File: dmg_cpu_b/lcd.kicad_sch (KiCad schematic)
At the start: 120 parts

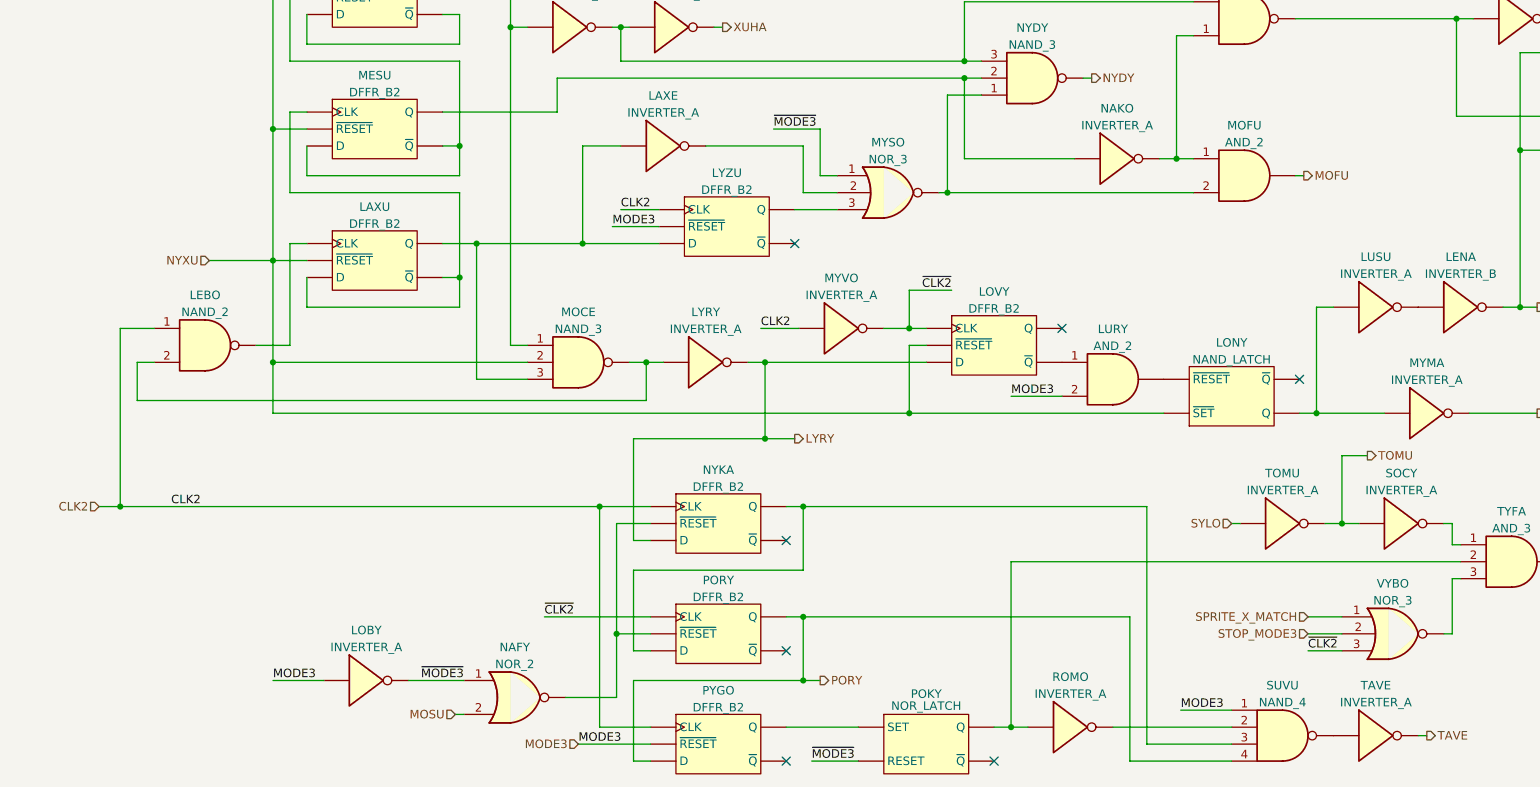
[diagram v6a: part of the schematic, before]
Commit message: More OAM sheets added.
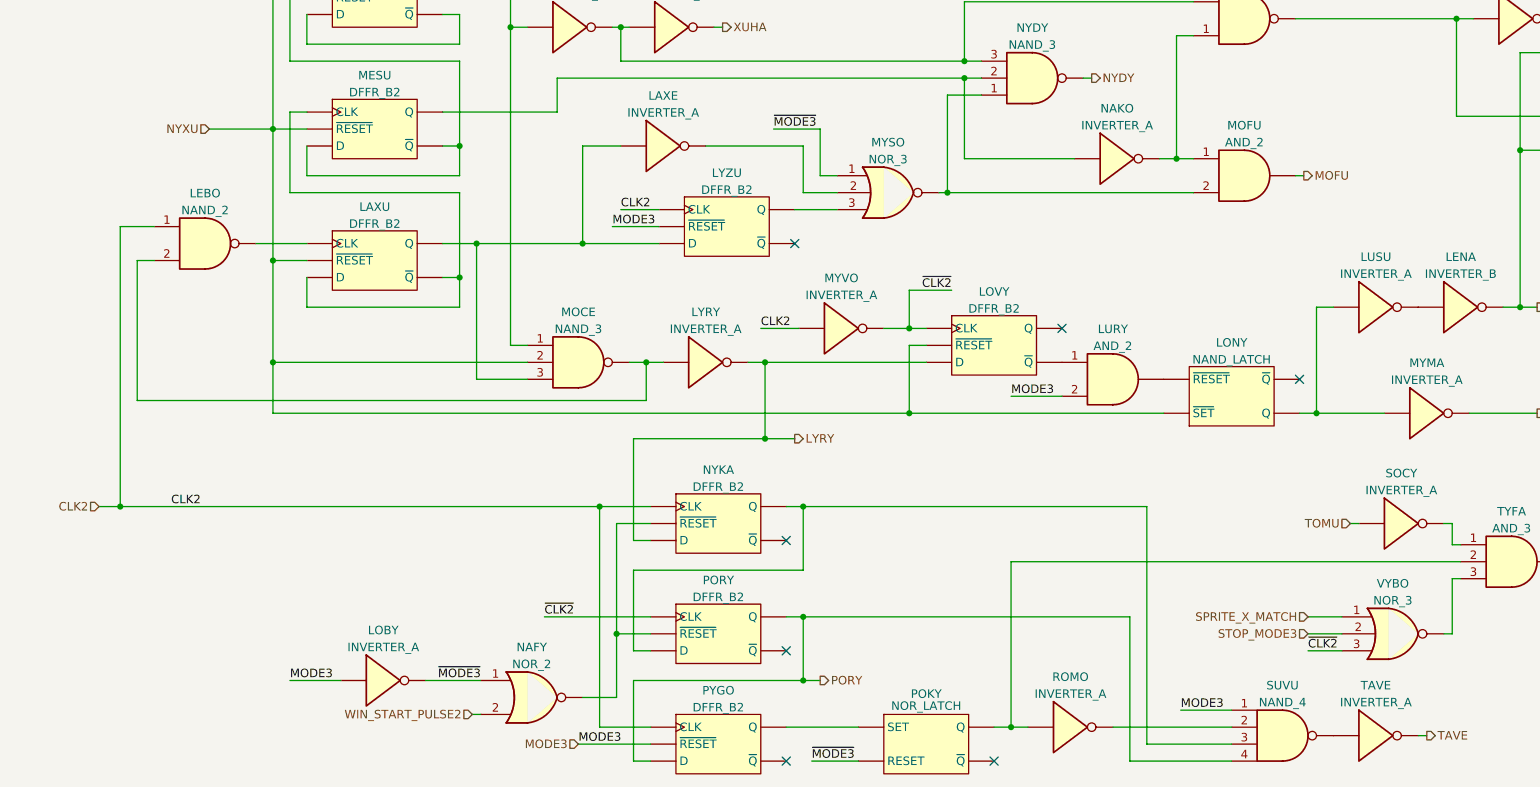
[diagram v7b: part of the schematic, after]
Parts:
- removed TOMU: INVERTER_A, symbol DMG_CPU_Cells:INVERTER_A
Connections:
- net MOSU renamed WIN_START_PULSE2
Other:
- moved on the sheet: LEBO, LOBY, NAFY
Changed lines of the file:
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@@
   (junction (at 331.47 94.615) (diameter 0) (color 0 0 0 0)
   )
-  (junction (at 208.28 245.745) (diameter 0) (color 0 0 0 0)
-  )
   (junction (at 127.635 269.24) (diameter 0) (color 0 0 0 0)
   )
@@
     (stroke (width 0) (type default) (color 0 0 0 0))
   )
-  (wire (pts (xy 50.8 203.835) (xy 50.8 219.075))
-    (stroke (width 0) (type default) (color 0 0 0 0))
-  )
   (wire (pts (xy 124.46 121.285) (xy 129.54 121.285))
     (stroke (width 0) (type default) (color 0 0 0 0))
@@
     (stroke (width 0) (type default) (color 0 0 0 0))
   )
-  (wire (pts (xy 76.835 274.32) (xy 75.565 274.32))
+  (wire (pts (xy 79.375 274.32) (xy 78.105 274.32))
     (stroke (width 0) (type default) (color 0 0 0 0))
   )
@@
     (stroke (width 0) (type default) (color 0 0 0 0))
   )
-  (wire (pts (xy 27.94 221.615) (xy 27.94 227.33))
+  (wire (pts (xy 27.94 206.375) (xy 27.94 227.33))
     (stroke (width 0) (type default) (color 0 0 0 0))
   )
@@
     (stroke (width 0) (type default) (color 0 0 0 0))
   )
-  (wire (pts (xy 38.735 206.375) (xy 48.26 206.375))
+  (wire (pts (xy 38.735 186.69) (xy 48.26 186.69))
     (stroke (width 0) (type default) (color 0 0 0 0))
   )
@@
     (stroke (width 0) (type default) (color 0 0 0 0))
   )
-  (wire (pts (xy 30.48 221.615) (xy 27.94 221.615))
+  (wire (pts (xy 30.48 206.375) (xy 27.94 206.375))
     (stroke (width 0) (type default) (color 0 0 0 0))
   )
@@
     (stroke (width 0) (type default) (color 0 0 0 0))
   )
-  (wire (pts (xy 208.28 245.745) (xy 210.82 245.745))
-    (stroke (width 0) (type default) (color 0 0 0 0))
-  )
   (wire (pts (xy 351.79 212.09) (xy 351.79 231.14))
     (stroke (width 0) (type default) (color 0 0 0 0))
@@
     (stroke (width 0) (type default) (color 0 0 0 0))
   )
-  (wire (pts (xy 53.34 203.835) (xy 50.8 203.835))
-    (stroke (width 0) (type default) (color 0 0 0 0))
-  )
   (wire (pts (xy 83.82 171.45) (xy 83.82 219.075))
     (stroke (width 0) (type default) (color 0 0 0 0))
@@
     (stroke (width 0) (type default) (color 0 0 0 0))
   )
-  (wire (pts (xy 191.77 245.745) (xy 193.04 245.745))
-    (stroke (width 0) (type default) (color 0 0 0 0))
-  )
   (wire (pts (xy 85.09 130.175) (xy 85.09 144.145))
     (stroke (width 0) (type default) (color 0 0 0 0))
@@
     (stroke (width 0) (type default) (color 0 0 0 0))
   )
-  (wire (pts (xy 208.28 235.585) (xy 212.09 235.585))
+  (wire (pts (xy 209.55 245.745) (xy 210.82 245.745))
     (stroke (width 0) (type default) (color 0 0 0 0))
   )
@@
     (stroke (width 0) (type default) (color 0 0 0 0))
   )
-  (wire (pts (xy 48.26 186.69) (xy 48.26 206.375))
-    (stroke (width 0) (type default) (color 0 0 0 0))
-  )
-  (wire (pts (xy 25.4 216.535) (xy 30.48 216.535))
+  (wire (pts (xy 25.4 201.295) (xy 30.48 201.295))
     (stroke (width 0) (type default) (color 0 0 0 0))
   )
@@
     (stroke (width 0) (type default) (color 0 0 0 0))
   )
-  (wire (pts (xy 92.075 271.78) (xy 99.695 271.78))
+  (wire (pts (xy 94.615 271.78) (xy 99.695 271.78))
     (stroke (width 0) (type default) (color 0 0 0 0))
   )
@@
     (stroke (width 0) (type default) (color 0 0 0 0))
   )
-  (wire (pts (xy 68.58 269.24) (xy 76.835 269.24))
+  (wire (pts (xy 71.12 269.24) (xy 79.375 269.24))
     (stroke (width 0) (type default) (color 0 0 0 0))
   )
@@
     (stroke (width 0) (type default) (color 0 0 0 0))
   )
-  (wire (pts (xy 50.8 219.075) (xy 45.72 219.075))
+  (wire (pts (xy 45.72 203.835) (xy 53.34 203.835))
     (stroke (width 0) (type default) (color 0 0 0 0))
   )
@@
     (stroke (width 0) (type default) (color 0 0 0 0))
   )
-  (wire (pts (xy 208.28 235.585) (xy 208.28 245.745))
-    (stroke (width 0) (type default) (color 0 0 0 0))
-  )
   (wire (pts (xy 183.515 88.9) (xy 183.515 128.27))
     (stroke (width 0) (type default) (color 0 0 0 0))
@@
     (stroke (width 0) (type default) (color 0 0 0 0))
   )
+  (wire (pts (xy 48.26 186.69) (xy 48.26 206.375))
+    (stroke (width 0) (type default) (color 0 0 0 0))
+  )
   (wire (pts (xy 186.055 196.215) (xy 149.225 196.215))
     (stroke (width 0) (type default) (color 0 0 0 0))
@@
     (stroke (width 0) (type default) (color 0 0 0 0))
   )
-  (wire (pts (xy 25.4 216.535) (xy 25.4 243.205))
+  (wire (pts (xy 25.4 201.295) (xy 25.4 243.205))
     (stroke (width 0) (type default) (color 0 0 0 0))
   )
@@
     (stroke (width 0) (type default) (color 0 0 0 0))
   )
-  (wire (pts (xy 205.74 245.745) (xy 208.28 245.745))
-    (stroke (width 0) (type default) (color 0 0 0 0))
-  )
   (wire (pts (xy 281.305 128.905) (xy 278.765 128.905))
     (stroke (width 0) (type default) (color 0 0 0 0))
@@
     (stroke (width 0) (type default) (color 0 0 0 0))
   )
-  (wire (pts (xy 48.26 269.24) (xy 55.88 269.24))
+  (wire (pts (xy 50.8 269.24) (xy 58.42 269.24))
     (stroke (width 0) (type default) (color 0 0 0 0))
   )
@@
     (effects (font (size 1.27 1.27)) (justify left bottom))
   )
-  (label "~{MODE3}" (at 76.835 269.24 180)
+  (label "~{MODE3}" (at 79.375 269.24 180)
     (effects (font (size 1.27 1.27)) (justify right bottom))
   )
@@
     (effects (font (size 1.27 1.27)) (justify left bottom))
   )
-  (label "MODE3" (at 48.26 269.24 0)
+  (label "MODE3" (at 50.8 269.24 0)
     (effects (font (size 1.27 1.27)) (justify left bottom))
   )
@@
     (effects (font (size 1.27 1.27)) (justify left bottom))
   )
-  (hierarchical_label "MOSU" (shape input) (at 75.565 274.32 180)
+  (hierarchical_label "WIN_START_PULSE2" (shape input) (at 78.105 274.32 180)
     (effects (font (size 1.27 1.27)) (justify right))
   )
@@
     (effects (font (size 1.27 1.27)) (justify right))
   )
-  (hierarchical_label "SYLO" (shape input) (at 191.77 245.745 180)
-    (effects (font (size 1.27 1.27)) (justify right))
-  )
   (hierarchical_label "CLKPIPE" (shape output) (at 279.4 254 0)
     (effects (font (size 1.27 1.27)) (justify left))
@@
     (effects (font (size 1.27 1.27)) (justify right))
   )
-  (hierarchical_label "NYXU" (shape input) (at 38.735 206.375 180)
+  (hierarchical_label "NYXU" (shape input) (at 38.735 186.69 180)
     (effects (font (size 1.27 1.27)) (justify right))
   )
@@
     (effects (font (size 1.27 1.27)) (justify left))
   )
-  (hierarchical_label "TOMU" (shape output) (at 212.09 235.585 0)
-    (effects (font (size 1.27 1.27)) (justify left))
+  (hierarchical_label "TOMU" (shape input) (at 209.55 245.745 180)
+    (effects (font (size 1.27 1.27)) (justify right))
   )
   (hierarchical_label "~{V_RESET}" (shape output) (at 314.96 22.225 0)
@@
     (pin "2")
   )
-  (symbol (lib_id "DMG_CPU_Cells:INVERTER_A") (at 199.39 245.745 0) (unit 1)
-    (in_bom yes) (on_board yes) (fields_autoplaced)
-    (property "Reference" "TOMU" (id 0) (at 199.39 238.2352 0))
-    (property "Value" "INVERTER_A" (id 1) (at 199.39 240.7721 0))
-    (property "Footprint" "" (id 2) (at 196.85 245.745 0)
-      (effects (font (size 1.27 1.27)) hide)
-    )
-    (property "Datasheet" "http://iceboy.a-singer.de/doc/dmg_cells.html#inv_a" (id 3) (at 200.66 253.365 0)
-      (effects (font (size 1.27 1.27)) hide)
-    )
-    (pin "1")
-    (pin "2")
-  )
   (symbol (lib_id "DMG_CPU_Cells:INVERTER_A") (at 314.325 119.38 0) (unit 1)
     (in_bom yes) (on_board yes)
@@
     (pin "6")
   )
-  (symbol (lib_id "DMG_CPU_Cells:INVERTER_A") (at 62.23 269.24 0) (unit 1)
+  (symbol (lib_id "DMG_CPU_Cells:INVERTER_A") (at 64.77 269.24 0) (unit 1)
     (in_bom yes) (on_board yes)
-    (property "Reference" "LOBY" (id 0) (at 62.23 261.7302 0))
-    (property "Value" "INVERTER_A" (id 1) (at 62.23 264.2671 0))
-    (property "Footprint" "" (id 2) (at 59.69 269.24 0)
+    (property "Reference" "LOBY" (id 0) (at 64.77 261.7302 0))
+    (property "Value" "INVERTER_A" (id 1) (at 64.77 264.2671 0))
+    (property "Footprint" "" (id 2) (at 62.23 269.24 0)
       (effects (font (size 1.27 1.27)) hide)
     )
-    (property "Datasheet" "http://iceboy.a-singer.de/doc/dmg_cells.html#inv_a" (id 3) (at 63.5 276.86 0)
+    (property "Datasheet" "http://iceboy.a-singer.de/doc/dmg_cells.html#inv_a" (id 3) (at 66.04 276.86 0)
       (effects (font (size 1.27 1.27)) hide)
     )
@@
     (pin "2")
   )
-  (symbol (lib_id "DMG_CPU_Cells:NAND_2") (at 38.1 219.075 0) (unit 1)
+  (symbol (lib_id "DMG_CPU_Cells:NAND_2") (at 38.1 203.835 0) (unit 1)
     (in_bom yes) (on_board yes) (fields_autoplaced)
-    (property "Reference" "LEBO" (id 0) (at 38.1 211.5652 0))
-    (property "Value" "NAND_2" (id 1) (at 38.1 214.1021 0))
-    (property "Footprint" "" (id 2) (at 38.1 219.075 0)
+    (property "Reference" "LEBO" (id 0) (at 38.1 196.3252 0))
+    (property "Value" "NAND_2" (id 1) (at 38.1 198.8621 0))
+    (property "Footprint" "" (id 2) (at 38.1 203.835 0)
       (effects (font (size 1.27 1.27)) hide)
     )
-    (property "Datasheet" "http://iceboy.a-singer.de/doc/dmg_cells.html#nand2" (id 3) (at 38.1 226.695 0)
+    (property "Datasheet" "http://iceboy.a-singer.de/doc/dmg_cells.html#nand2" (id 3) (at 38.1 211.455 0)
       (effects (font (size 1.27 1.27)) hide)
     )
@@
     (pin "5")
   )
-  (symbol (lib_id "DMG_CPU_Cells:NOR_2") (at 84.455 271.78 0) (unit 1)
+  (symbol (lib_id "DMG_CPU_Cells:NOR_2") (at 86.995 271.78 0) (unit 1)
     (in_bom yes) (on_board yes) (fields_autoplaced)
-    (property "Reference" "NAFY" (id 0) (at 84.4548 264.2702 0))
-    (property "Value" "NOR_2" (id 1) (at 84.4548 266.8071 0))
-    (property "Footprint" "" (id 2) (at 84.201 271.78 0)
+    (property "Reference" "NAFY" (id 0) (at 86.9948 264.2702 0))
+    (property "Value" "NOR_2" (id 1) (at 86.9948 266.8071 0))
+    (property "Footprint" "" (id 2) (at 86.741 271.78 0)
       (effects (font (size 1.27 1.27)) hide)
     )
-    (property "Datasheet" "http://iceboy.a-singer.de/doc/dmg_cells.html#nor2" (id 3) (at 84.455 279.4 0)
+    (property "Datasheet" "http://iceboy.a-singer.de/doc/dmg_cells.html#nor2" (id 3) (at 86.995 279.4 0)
       (effects (font (size 1.27 1.27)) hide)
     )

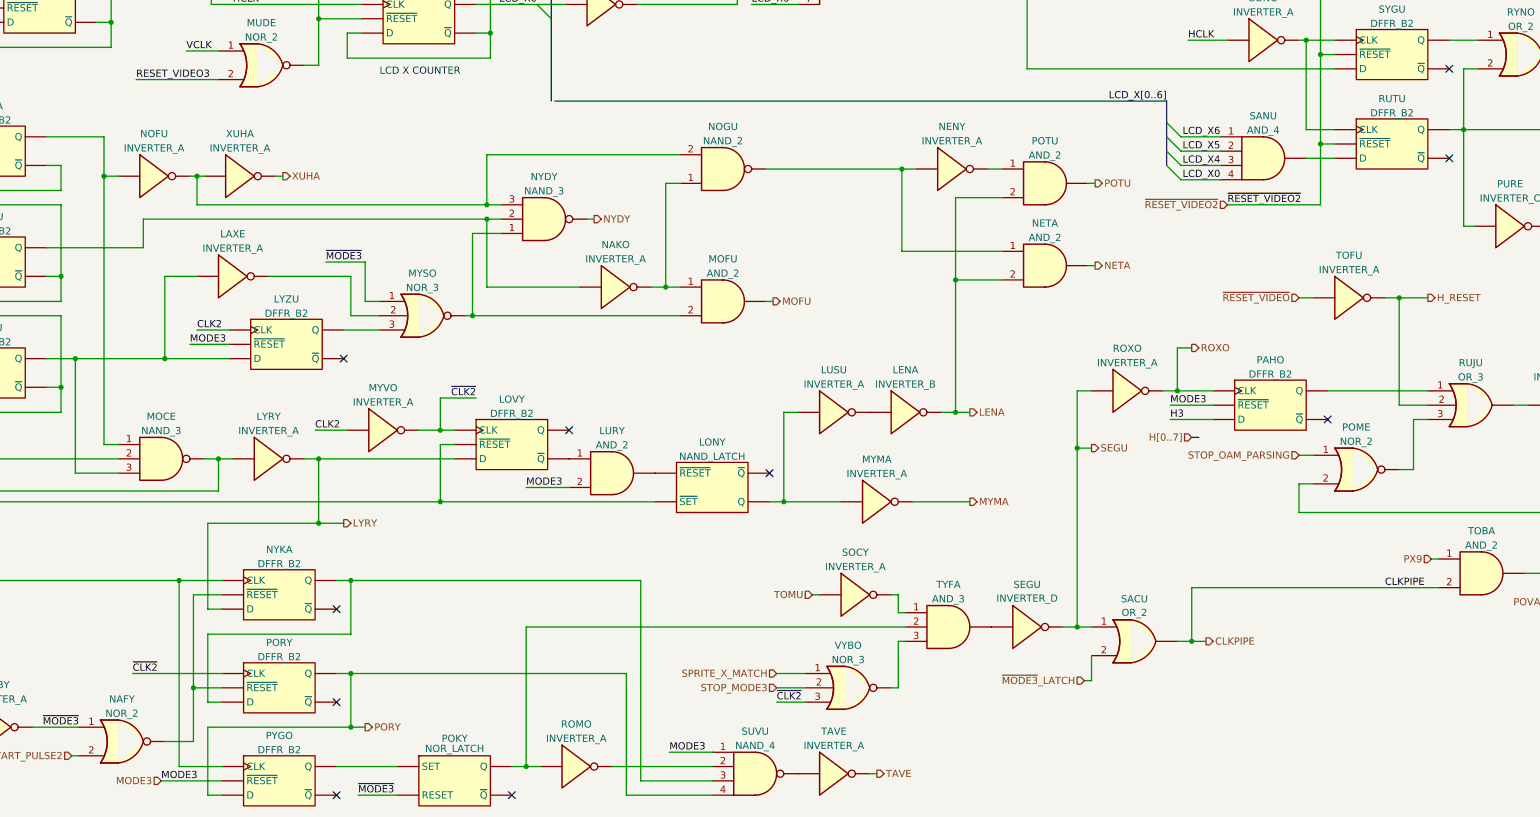
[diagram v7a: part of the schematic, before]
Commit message: All sheets captured. Serious tidying is required in PPU section.
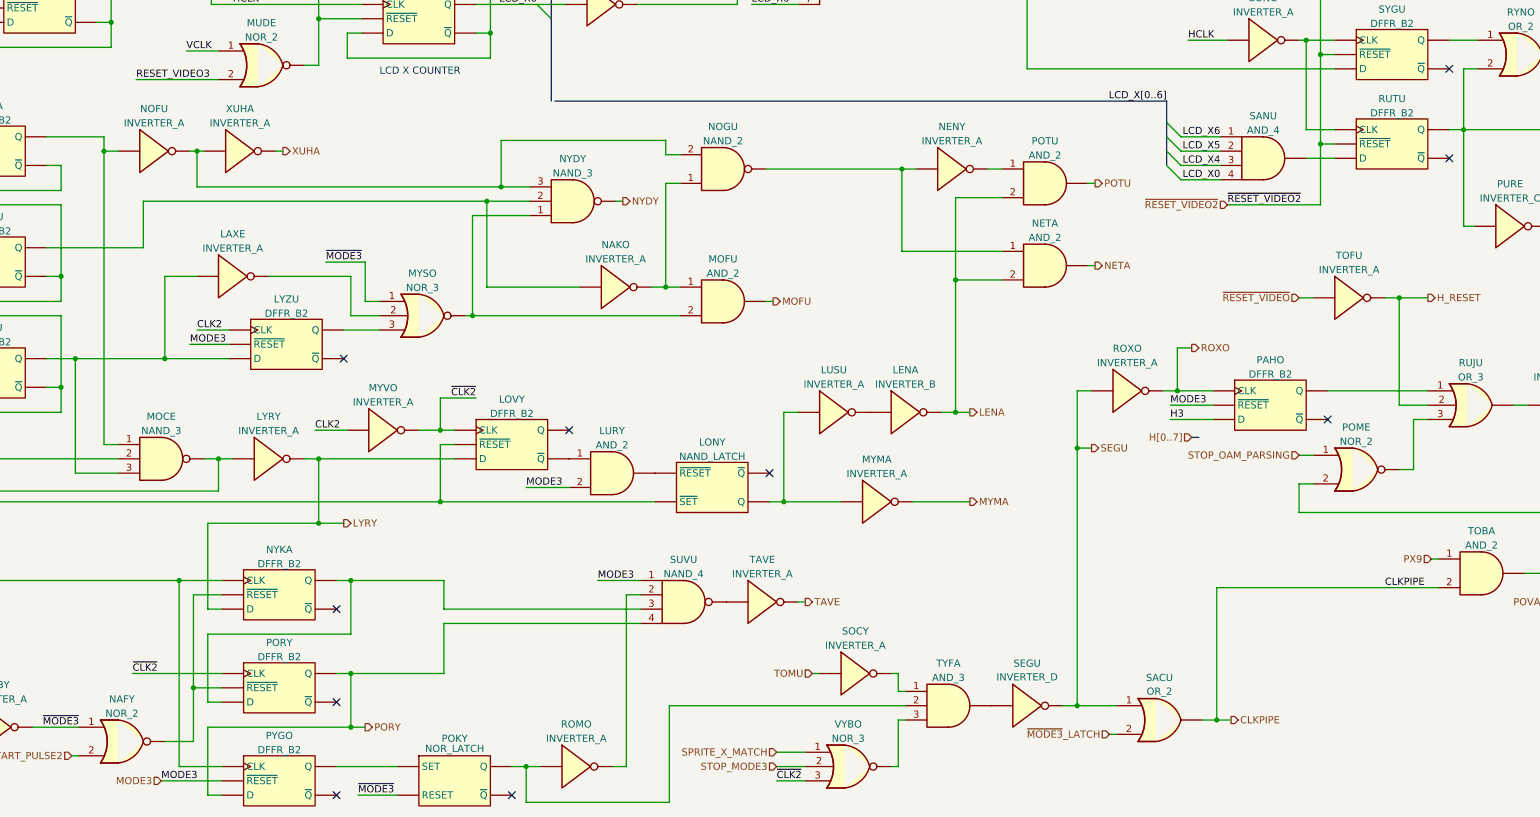
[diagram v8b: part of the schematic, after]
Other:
- moved on the sheet: NOFU, NYDY, SACU, SEGU, SOCY, SUVU, TAVE, TYFA, VYBO, XUHA
